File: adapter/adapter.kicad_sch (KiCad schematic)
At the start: 23 parts, among them J1 Conn_01x01_Female, J2 Conn_01x06_Female, J3 Conn_01x01_Female, J4 Conn_01x01_Female, J5 Conn_01x01_Female, SW1 RotaryEncoder_Switch

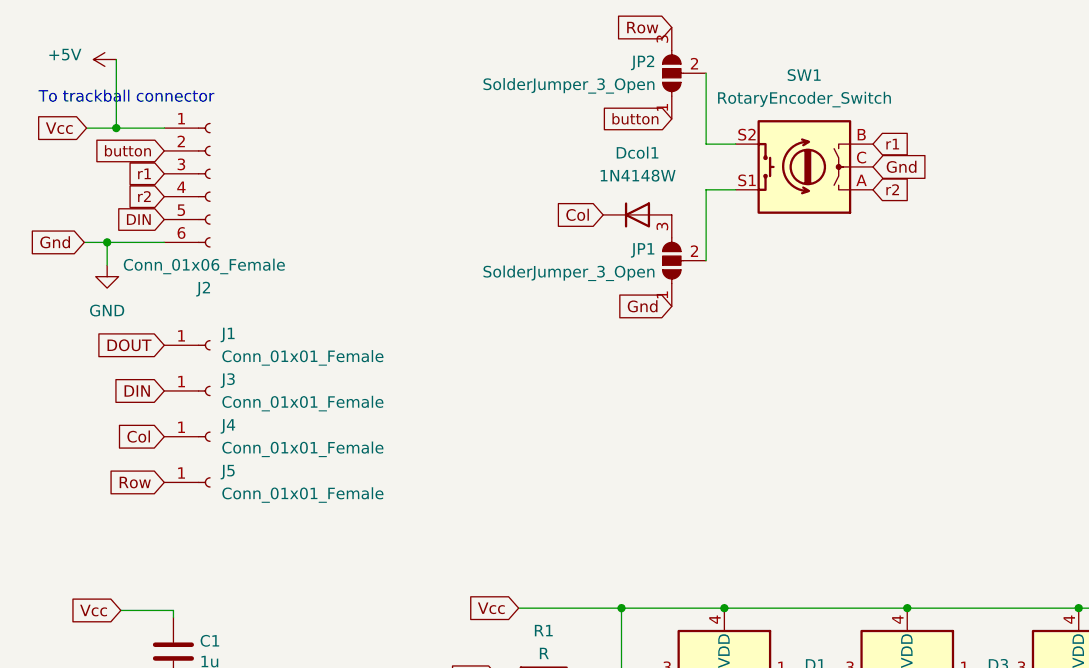
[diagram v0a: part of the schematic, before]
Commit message: rearranged pins and reroute
reverted BK logo to silkscreen
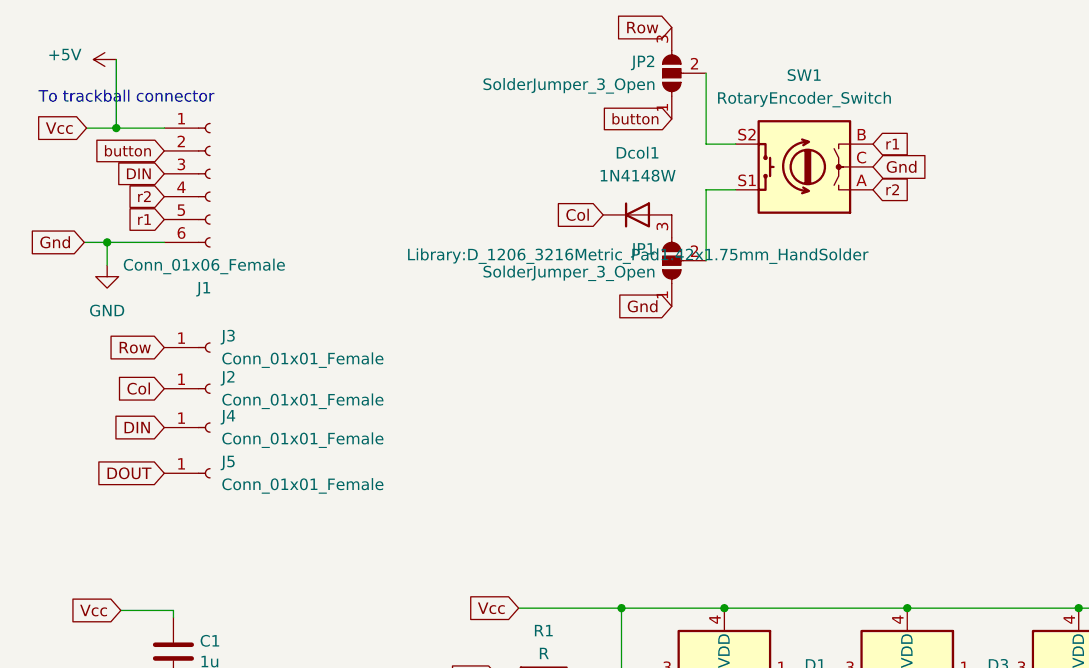
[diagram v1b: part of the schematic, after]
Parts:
- Dcol1: footprint Library:D_SOD-123 -> Library:D_1206_3216Metric_Pad1.42x1.75mm_HandSolder
- renumbered J2 to J1, J1 to J2, J5 to J3, J3 to J4, J4 to J5
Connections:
- net Col: now also J2.1 (Pin_1); no longer J5.1 (Pin_1)
- net DIN: now also J1.3 (Pin_3); no longer J1.5 (Pin_5)
- net DOUT: now also J5.1 (Pin_1); no longer J2.1 (Pin_1)
- net r1: now also J1.5 (Pin_5); no longer J1.3 (Pin_3)
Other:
- moved on the sheet: J2, J3, J4, J5

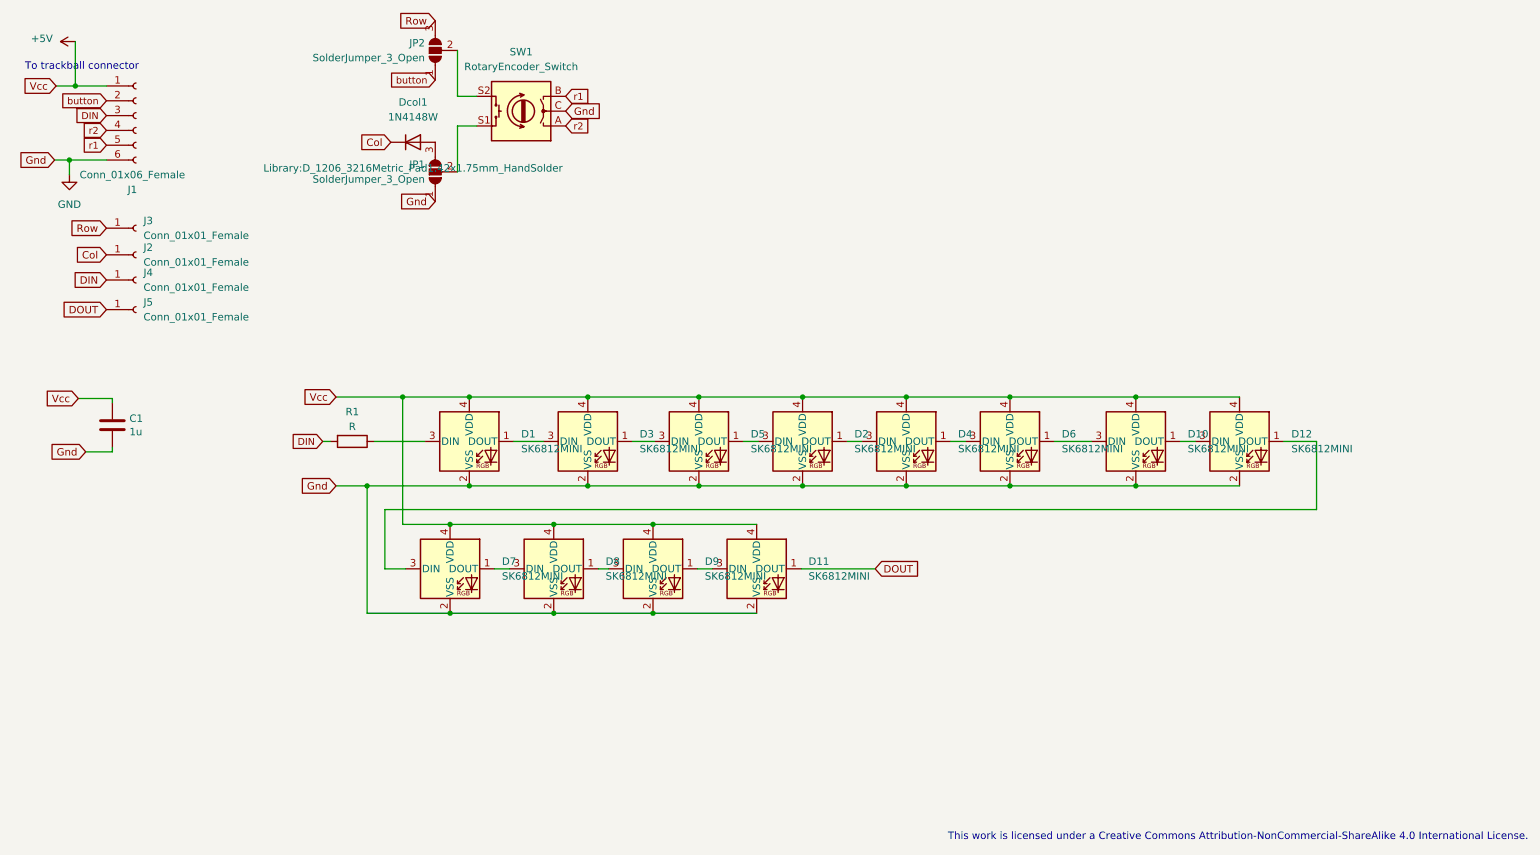
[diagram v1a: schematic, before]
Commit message: flip LEDs to correct orientation
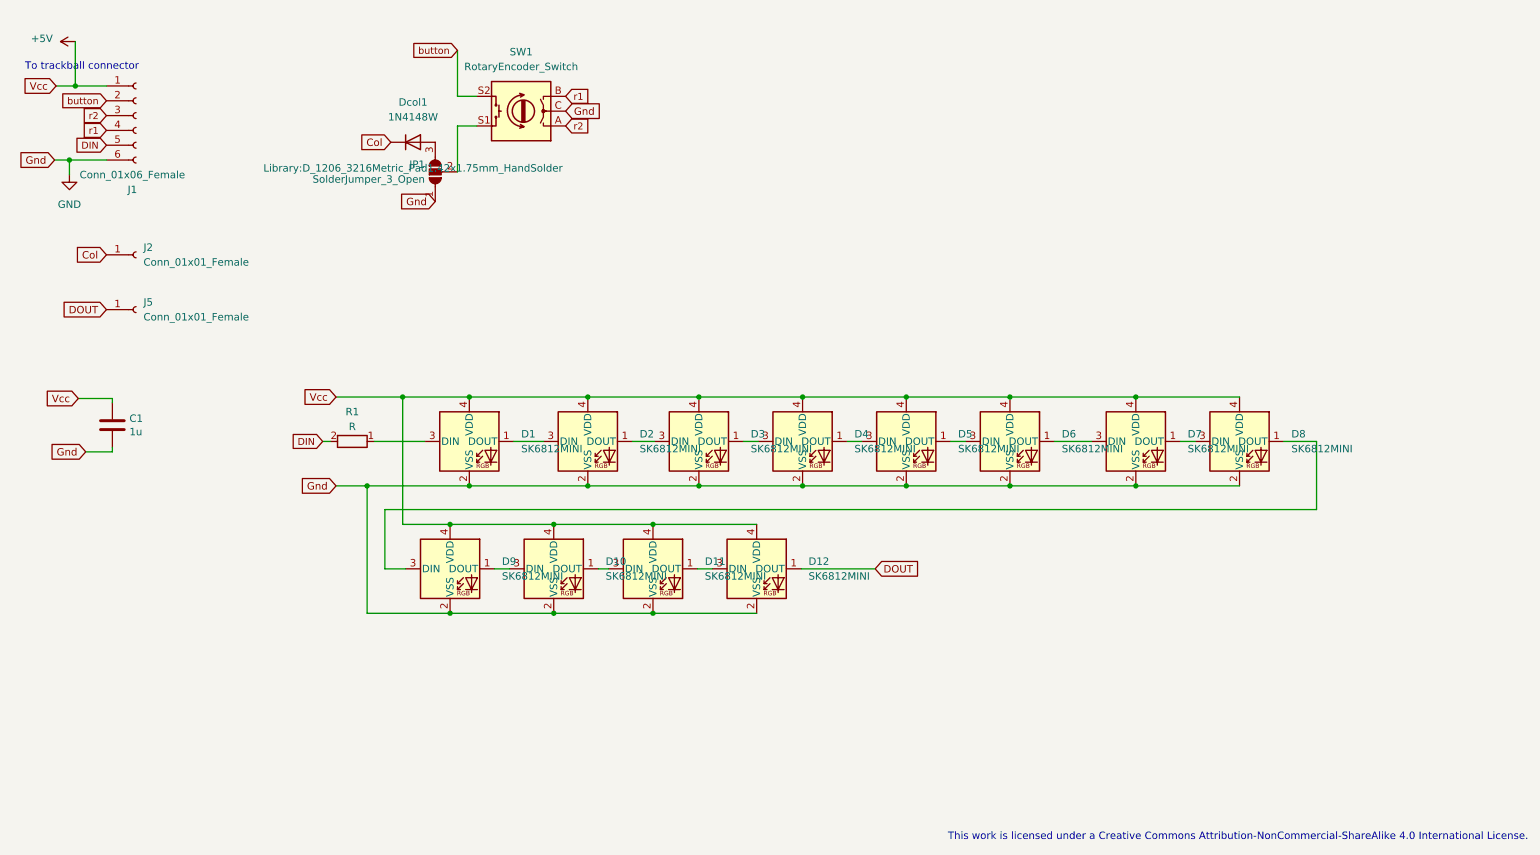
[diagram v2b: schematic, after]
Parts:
- removed J3, J4: Conn_01x01_Female, Library:1_PinHeader, symbol Connector:Conn_01x01_Female
- removed JP2: SolderJumper_3_Open, Library:SolderJumper-3_P1.3mm_Open_RoundedPad1.0x1.5mm reversed, symbol Jumper:SolderJumper_3_Open
- renumbered D8 to D10, D9 to D11, D11 to D12, D3 to D2, D5 to D3, D2 to D4, D4 to D5, D10 to D7, D12 to D8, D7 to D9
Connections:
- net DIN: now also J1.5 (Pin_5); no longer J1.3 (Pin_3)
- net button: now also SW1.S2
- net r1: now also J1.4 (Pin_4); no longer J1.5 (Pin_5)
- net r2: now also J1.3 (Pin_3); no longer J1.4 (Pin_4)

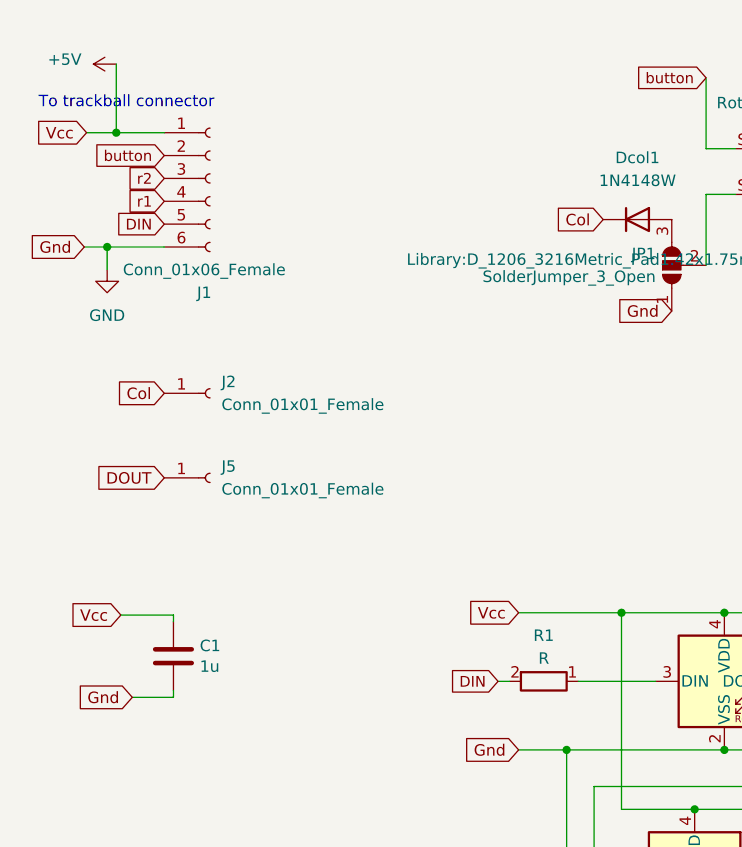
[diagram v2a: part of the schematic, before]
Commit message: added power flags to resolve erc error
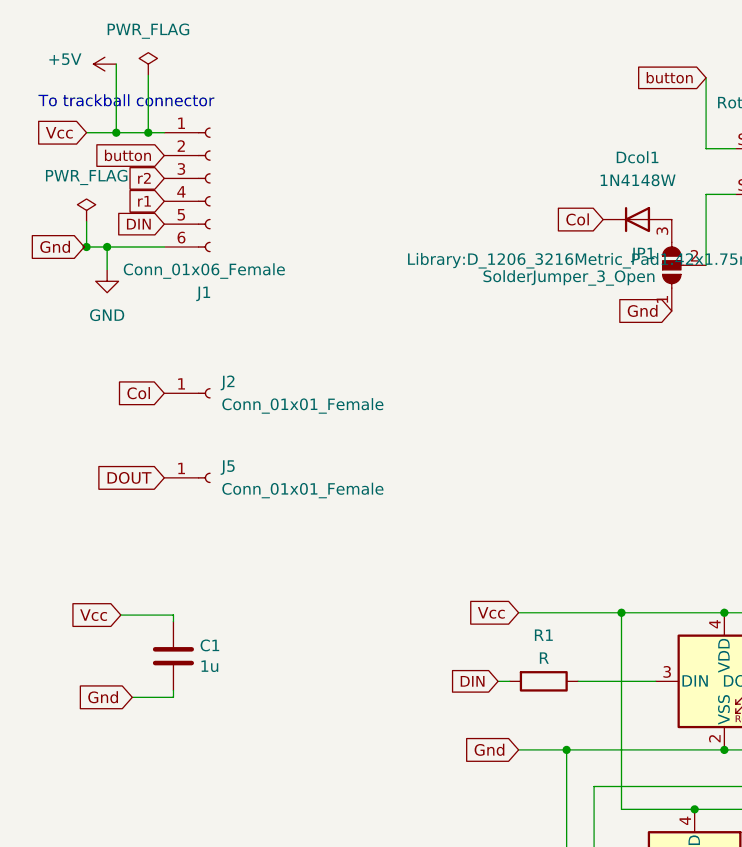
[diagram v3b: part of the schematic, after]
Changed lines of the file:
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@@
   (junction (at 80.264 102.87) (diameter 0) (color 0 0 0 0)
   )
+  (junction (at 33.782 34.29) (diameter 0) (color 0 0 0 0)
+  )
   (junction (at 112.268 124.714) (diameter 0) (color 0 0 0 0)
   )
+  (junction (at 26.924 46.99) (diameter 0) (color 0 0 0 0)
+  )
   (junction (at 212.09 87.63) (diameter 0) (color 0 0 0 0)
   )
@@
   )
   (wire (pts (xy 162.56 95.25) (xy 165.1 95.25))
+    (stroke (width 0) (type default) (color 0 0 0 0))
+  )
+  (wire (pts (xy 26.924 44.196) (xy 26.924 46.99))
     (stroke (width 0) (type default) (color 0 0 0 0))
   )
@@
     (stroke (width 0) (type default) (color 0 0 0 0))
   )
-  (wire (pts (xy 30.226 34.29) (xy 35.56 34.29))
+  (wire (pts (xy 30.226 34.29) (xy 33.782 34.29))
     (stroke (width 0) (type default) (color 0 0 0 0))
   )
@@
     (stroke (width 0) (type default) (color 0 0 0 0))
   )
-  (wire (pts (xy 26.67 46.99) (xy 29.21 46.99))
+  (wire (pts (xy 26.67 46.99) (xy 26.924 46.99))
     (stroke (width 0) (type default) (color 0 0 0 0))
   )
@@
     (stroke (width 0) (type default) (color 0 0 0 0))
   )
+  (wire (pts (xy 33.782 34.29) (xy 35.56 34.29))
+    (stroke (width 0) (type default) (color 0 0 0 0))
+  )
   (wire (pts (xy 29.21 46.99) (xy 29.21 49.53))
     (stroke (width 0) (type default) (color 0 0 0 0))
@@
   )
   (wire (pts (xy 219.71 95.25) (xy 222.25 95.25))
+    (stroke (width 0) (type default) (color 0 0 0 0))
+  )
+  (wire (pts (xy 33.782 27.94) (xy 33.782 34.29))
     (stroke (width 0) (type default) (color 0 0 0 0))
   )
@@
   )
   (wire (pts (xy 86.36 109.474) (xy 94.488 109.474))
+    (stroke (width 0) (type default) (color 0 0 0 0))
+  )
+  (wire (pts (xy 26.924 46.99) (xy 29.21 46.99))
     (stroke (width 0) (type default) (color 0 0 0 0))
   )
@@
     (pin "4")
   )
+  (symbol (lib_id "power:PWR_FLAG") (at 33.782 27.94 0) (unit 1)
+    (in_bom yes) (on_board yes) (fields_autoplaced)
+    (property "Reference" "#FLG0102" (id 0) (at 33.782 26.035 0)
+      (effects (font (size 1.27 1.27)) hide)
+    )
+    (property "Value" "PWR_FLAG" (id 1) (at 33.782 22.86 0))
+    (property "Footprint" "" (id 2) (at 33.782 27.94 0)
+      (effects (font (size 1.27 1.27)) hide)
+    )
+    (property "Datasheet" "~" (id 3) (at 33.782 27.94 0)
+      (effects (font (size 1.27 1.27)) hide)
+    )
+    (pin "1")
+  )
   (symbol (lib_id "LED:SK6812MINI") (at 129.286 117.094 0) (unit 1)
     (in_bom yes) (on_board yes)
@@
     )
     (property "Datasheet" "" (id 3) (at 29.21 49.53 0)
+      (effects (font (size 1.27 1.27)) hide)
+    )
+    (pin "1")
+  )
+  (symbol (lib_id "power:PWR_FLAG") (at 26.924 44.196 0) (unit 1)
+    (in_bom yes) (on_board yes) (fields_autoplaced)
+    (property "Reference" "#FLG0101" (id 0) (at 26.924 42.291 0)
+      (effects (font (size 1.27 1.27)) hide)
+    )
+    (property "Value" "PWR_FLAG" (id 1) (at 26.924 39.116 0))
+    (property "Footprint" "" (id 2) (at 26.924 44.196 0)
+      (effects (font (size 1.27 1.27)) hide)
+    )
+    (property "Datasheet" "~" (id 3) (at 26.924 44.196 0)
       (effects (font (size 1.27 1.27)) hide)
     )
@@
   )
   (symbol_instances
+    (path "/ac7d251e-7c93-4c89-8467-ebd89d6ef6bb"
+      (reference "#FLG0101") (unit 1) (value "PWR_FLAG") (footprint "")
+    )
+    (path "/5b3d0377-820c-4868-8ab2-62f2ccecf4af"
+      (reference "#FLG0102") (unit 1) (value "PWR_FLAG") (footprint "")
+    )
     (path "/93a90ae2-756d-42f3-a28d-f6c41463f86e"
       (reference "#PWR0101") (unit 1) (value "+5V") (footprint "")
